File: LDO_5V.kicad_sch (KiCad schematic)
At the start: 0 parts

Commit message: progress on switch sheet
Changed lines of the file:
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@@
 	(paper "A4")
+	(rectangle
+		(start 147.32 109.22)
+		(end 170.18 127)
+		(stroke
+			(width 0)
+			(type default)
+		)
+		(fill
+			(type none)
+		)
+	)
 	(rectangle
 		(start 147.32 86.36)
@@
 	(text "LDO"
 		(exclude_from_sim no)
+		(at 159.004 118.364 0)
+		(effects
+			(font
+				(size 1.27 1.27)
+			)
+		)
+	)
+	(text "LDO"
+		(exclude_from_sim no)
 		(at 159.004 95.504 0)
 		(effects
@@
 		)
 	)
+	(text_box "Ouput current needed?"
+		(exclude_from_sim no)
+		(at 30.226 46.736 0)
+		(size 40.894 22.86)
+		(margins 0.9525 0.9525 0.9525 0.9525)
+		(stroke
+			(width 0)
+			(type solid)
+		)
+		(fill
+			(type none)
+		)
+		(effects
+			(font
+				(size 5 5)
+				(thickness 1)
+				(bold yes)
+				(color 255 0 19 1)
+			)
+			(justify left top)
+		)
+	)
 	(wire
 		(pts
@@
 		(pts
 			(xy 107.95 96.52) (xy 147.32 96.52)
+		)
+		(stroke
+			(width 0)
+			(type default)
+		)
+	)
+	(wire
+		(pts
+			(xy 170.18 119.38) (xy 204.47 119.38)
+		)
+		(stroke
+			(width 0)
+			(type default)
+		)
+	)
+	(wire
+		(pts
+			(xy 107.95 119.38) (xy 147.32 119.38)
 		)
 		(stroke
@@
 		)
 	)
+	(hierarchical_label "VOUT"
+		(shape output)
+		(at 204.47 119.38 0)
+		(effects
+			(font
+				(size 1.27 1.27)
+			)
+			(justify left)
+		)
+	)
+	(hierarchical_label "VIN"
+		(shape input)
+		(at 107.95 119.38 180)
+		(effects
+			(font
+				(size 1.27 1.27)
+			)
+			(justify right)
+		)
+	)

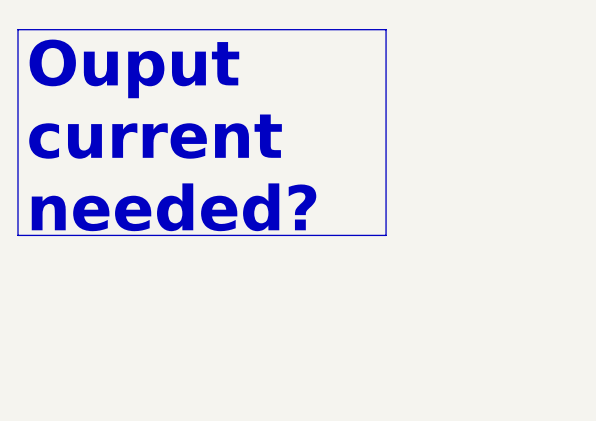
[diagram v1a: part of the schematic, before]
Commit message: specified parts and connection, updated notes
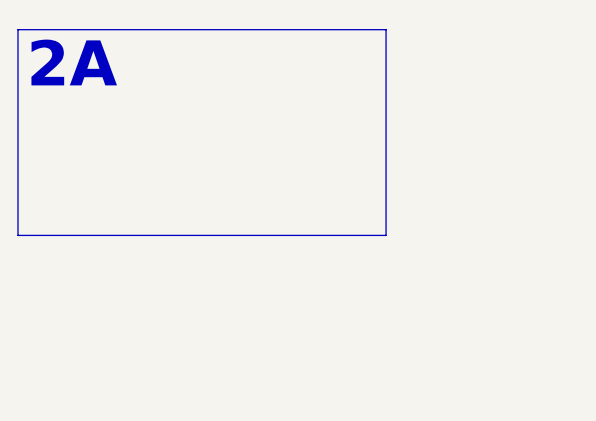
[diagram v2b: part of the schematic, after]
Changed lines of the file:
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@@
 		)
 	)
-	(text_box "Ouput current needed?"
+	(text_box "2A"
 		(exclude_from_sim no)
 		(at 30.226 46.736 0)

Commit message: specified design
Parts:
- added C1701, C1702, C1703, C1704, C1705, C1706: C_Small, Capacitor_SMD:C_0603_1608Metric_Pad1.08x0.95mm_HandSolder, symbol Device:C_Small
- added C1707, C1708: 100n, Capacitor_SMD:C_0603_1608Metric_Pad1.08x0.95mm_HandSolder, symbol Device:C_Small
- added C1709, C1710, C1713, C1714: 1u, Capacitor_SMD:C_0603_1608Metric_Pad1.08x0.95mm_HandSolder, symbol Device:C_Small
- added C1711, C1712: 10u, Capacitor_SMD:C_0603_1608Metric_Pad1.08x0.95mm_HandSolder, symbol Device:C_Small
- added L1701, L1702: L_Small, Inductor_SMD:L_Taiyo-Yuden_NR-10050_9.8x10.0mm_HandSoldering, symbol Device:L_Small
- added Q1701: NMOS, Package_TO_SOT_SMD:SOT-23, symbol Simulation_SPICE:NMOS
- added Q1702, Q1703: NMOS, Package_TO_SOT_SMD:SOT-23-6, symbol Simulation_SPICE:NMOS
- added R1701, R1702, R1703, R1704, R1705: R_Small, Resistor_SMD:R_0603_1608Metric_Pad0.98x0.95mm_HandSolder, symbol Device:R_Small
- added R1706, R1708: 52500, Resistor_SMD:R_0603_1608Metric_Pad0.98x0.95mm_HandSolder, symbol Device:R_Small
- added R1707, R1709: 10k, Resistor_SMD:R_0603_1608Metric_Pad0.98x0.95mm_HandSolder, symbol Device:R_Small
- added U1701, U1702: TPS62933, Package_TO_SOT_SMD:SOT-583-8, symbol Regulator_Switching:TPS62933
- added U1703, U1704: LM74700, Package_TO_SOT_SMD:SOT-23-6, symbol Power_Management:LM74700
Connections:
- net VIN: now also C1701.1, C1702.1, R1702.1, U1701.3 (VIN), U1702.3 (VIN)
- net VOUT: now also Q1702.1 (D), Q1703.1 (D), U1703.4 (CATHODE), U1704.4 (CATHODE)
- new net: C1706.1, U1702.6 (BST)
- new net: C1706.2, L1702.1, U1702.5 (SW)
- new net: R1704.2, U1701.1 (RT)
- new net: Q1701.1 (D), R1703.1
- new net: C1703.1, U1701.7 (SS)
- new net: C1707.1, C1709.1, C1711.1, C1713.1, L1701.2, Q1702.3 (S), R1701.1, R1706.2, U1703.3 (EN), U1703.6 (ANODE)
- new net: C1714.2, U1704.1 (VCAP)
- new net: C1708.1, C1710.1, C1712.1, C1714.1, L1702.2, Q1703.3 (S), R1708.2, U1704.3 (EN), U1704.6 (ANODE)
- new net: Q1703.2 (G), U1704.5 (GATE)
- new net: R1708.1, R1709.2, U1702.8 (FB)
- new net: C1705.2, L1701.1, U1701.5 (SW)
- new net: C1705.1, U1701.6 (BST)
- new net: R1706.1, R1707.2, U1701.8 (FB)
- new net: C1713.2, U1703.1 (VCAP)
- new net: R1705.2, U1702.1 (RT)
- new net: Q1701.3 (S), R1702.2, U1702.2 (EN)
- new net: Q1702.2 (G), U1703.5 (GATE)
- new net: C1704.1, U1702.7 (SS)
- new net: Q1701.2 (G), R1701.2
- new net EN: U1701.2 (EN)
- new net GND: C1701.2, C1702.2, C1703.2, C1704.2, C1707.2, C1708.2, C1709.2, C1710.2, C1711.2, C1712.2, R1703.2, R1704.1, R1705.1, R1707.1, R1709.1, U1701.4 (GND), U1702.4 (GND), U1703.2 (GND), U1704.2 (GND)
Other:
- note removed: "LDO"

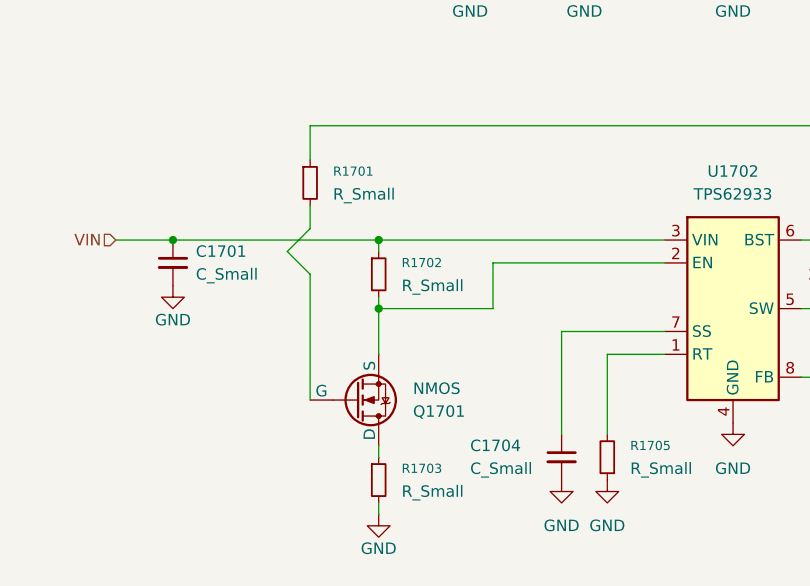
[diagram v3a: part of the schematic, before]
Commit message: added RS422, housekeeping
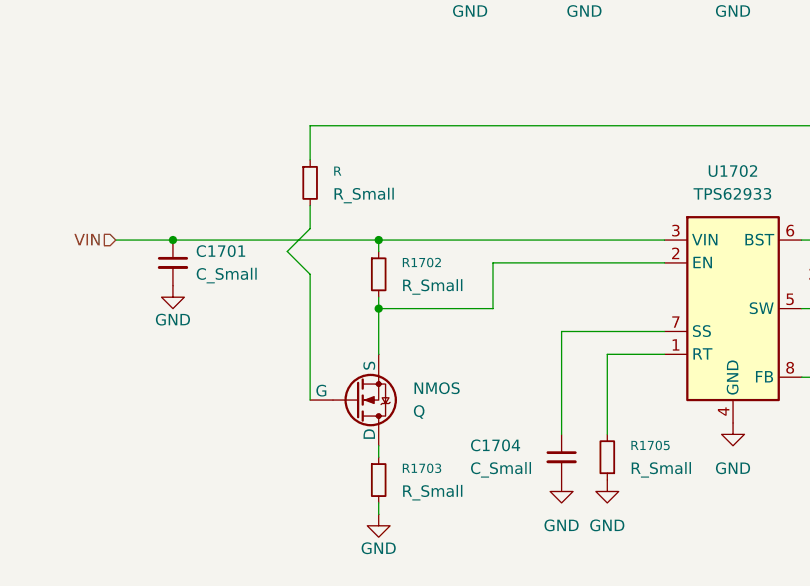
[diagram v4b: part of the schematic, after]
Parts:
- renumbered Q1701 to Q, R1701 to R

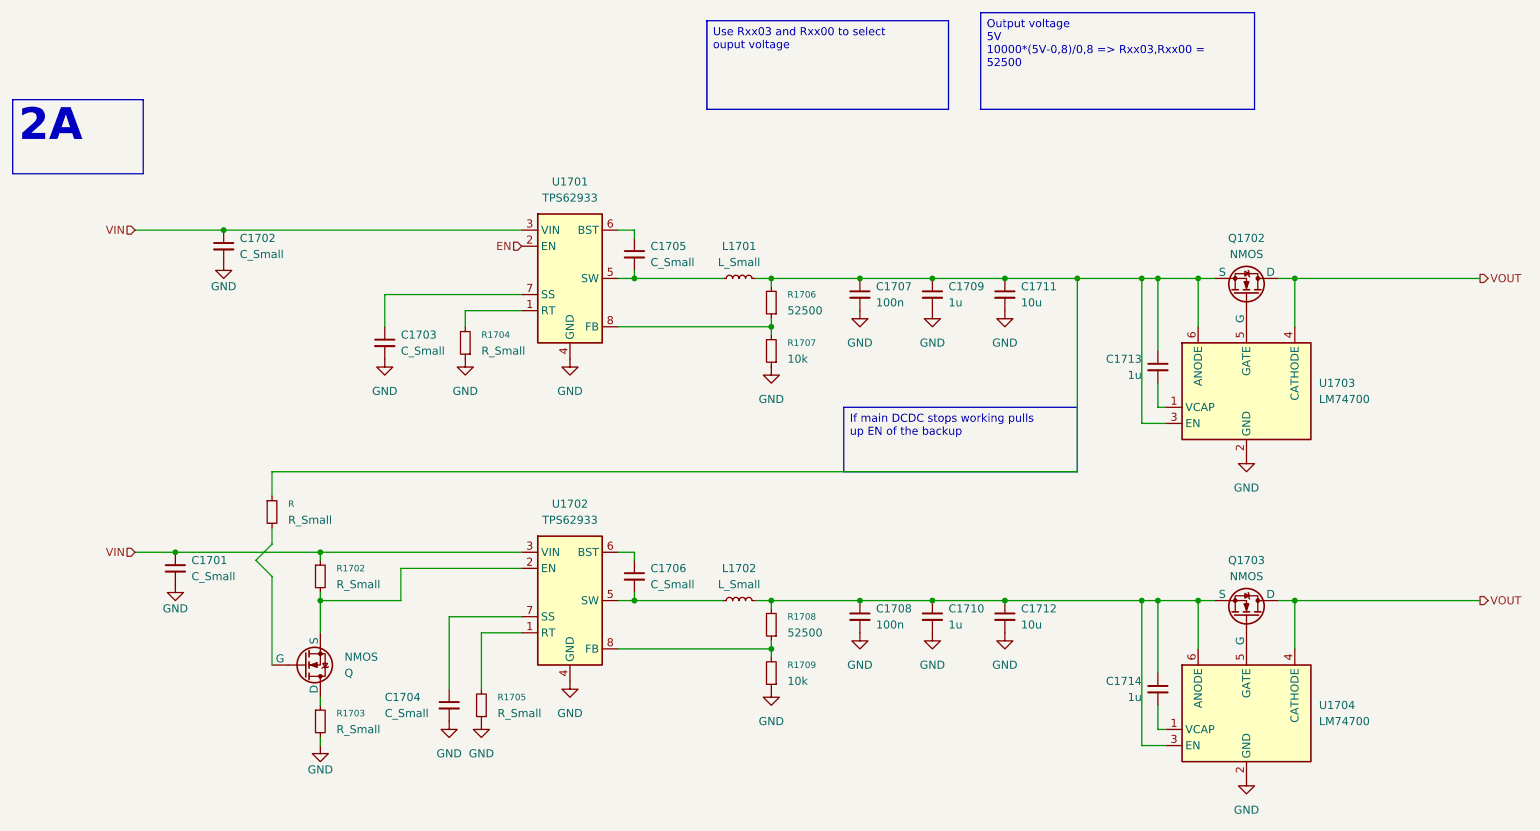
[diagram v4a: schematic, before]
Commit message: updated battery pack module; updated solar inputs module
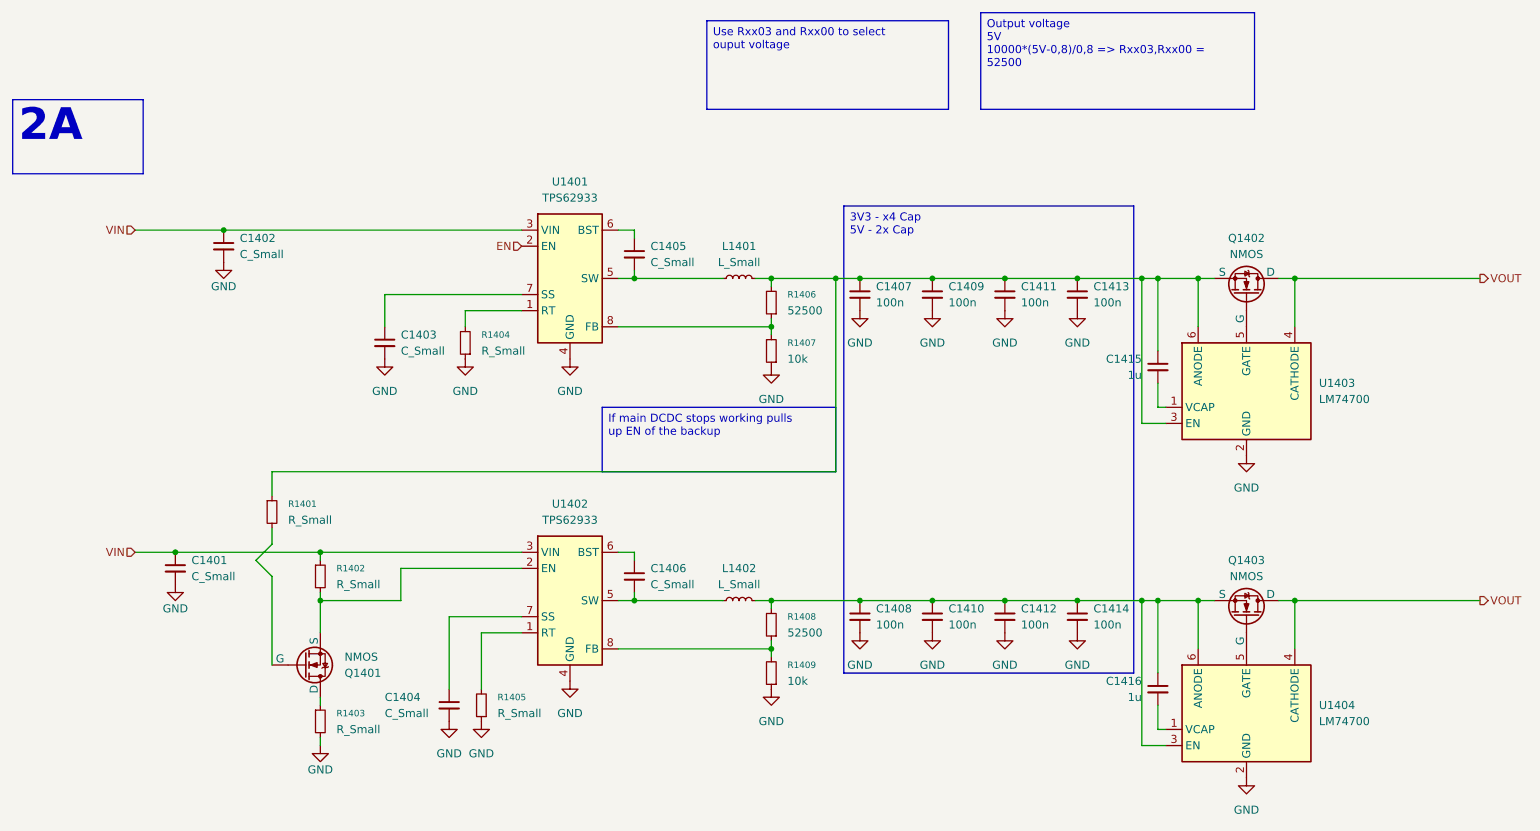
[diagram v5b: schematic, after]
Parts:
- removed C1709, C1710: 1u, Capacitor_SMD:C_0603_1608Metric_Pad1.08x0.95mm_HandSolder, symbol Device:C_Small
- removed C1711, C1712: 10u, Capacitor_SMD:C_0603_1608Metric_Pad1.08x0.95mm_HandSolder, symbol Device:C_Small
- added C1409, C1410, C1411, C1412, C1413, C1414: 100n, Capacitor_SMD:C_0603_1608Metric_Pad1.08x0.95mm_HandSolder, symbol Device:C_Small
- renumbered C1701 to C1401, C1702 to C1402, C1703 to C1403, C1704 to C1404, C1705 to C1405, C1706 to C1406, C1707 to C1407, C1708 to C1408, C1713 to C1415, C1714 to C1416, L1701 to L1401, L1702 to L1402, Q to Q1401, Q1702 to Q1402, Q1703 to Q1403, R to R1401, R1702 to R1402, R1703 to R1403, R1704 to R1404, R1705 to R1405, R1706 to R1406, R1707 to R1407, R1708 to R1408, R1709 to R1409, U1701 to U1401, U1702 to U1402, U1703 to U1403, U1704 to U1404
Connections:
- net GND: now also C1409.2, C1410.2, C1411.2, C1412.2, C1413.2, C1414.2
- net at C1407.1, C1415.1, L1401.2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: now also C1409.1, C1411.1, C1413.1
- net at C1408.1, C1416.1, L1402.2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: now also C1410.1, C1412.1, C1414.1

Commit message: added values to most parts
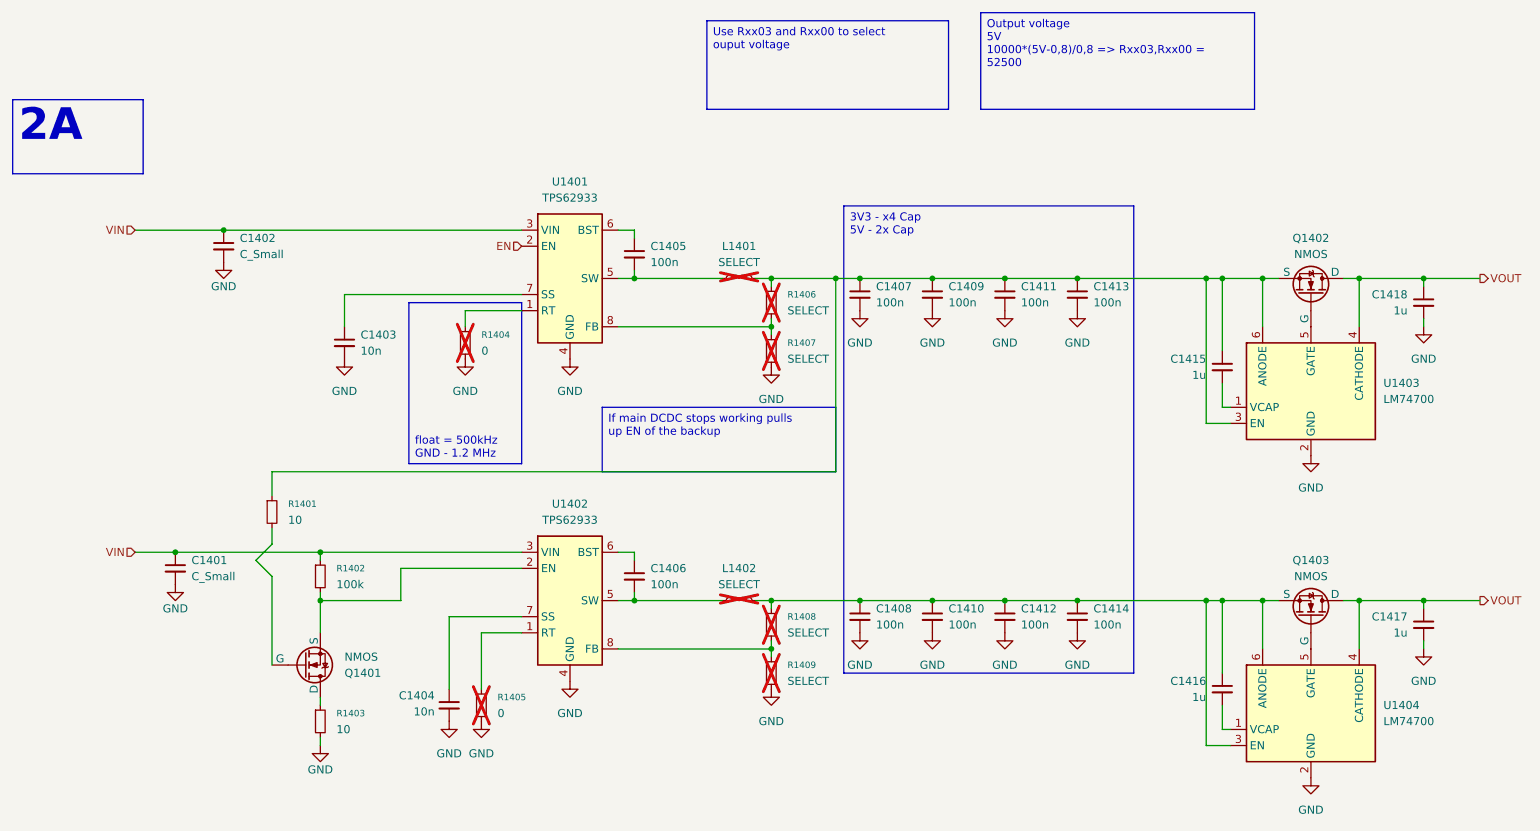
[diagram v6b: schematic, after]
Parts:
- added C1417, C1418: 1u, Capacitor_SMD:C_0603_1608Metric_Pad1.08x0.95mm_HandSolder, symbol Device:C_Small
- C1403, C1404: value C_Small -> 10n
- C1405, C1406: value C_Small -> 100n
- L1401, L1402: value L_Small -> SELECT; now not fitted
- R1401, R1403: value R_Small -> 10
- R1402: value R_Small -> 100k
- R1404, R1405: value R_Small -> 0; now not fitted
- R1406, R1408: value 52500 -> SELECT; now not fitted
- R1407, R1409: value 10k -> SELECT; now not fitted
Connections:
- net GND: now also C1417.2, C1418.2
- net VOUT: now also C1417.1, C1418.1
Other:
- moved on the sheet: C1403, C1415, C1416, Q1402, Q1403, U1403, U1404
